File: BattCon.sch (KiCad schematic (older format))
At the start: 31 parts

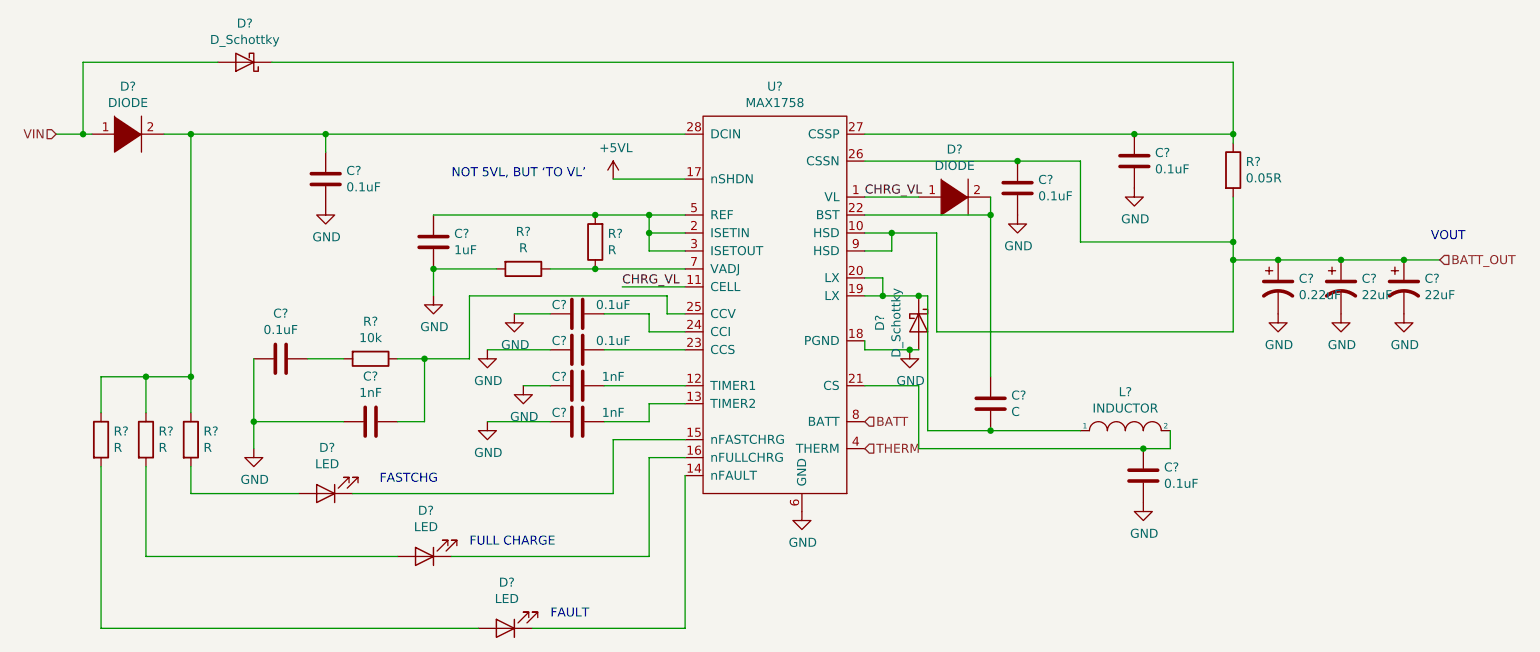
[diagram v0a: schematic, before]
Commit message: Schematics Done. Now need to do footprints
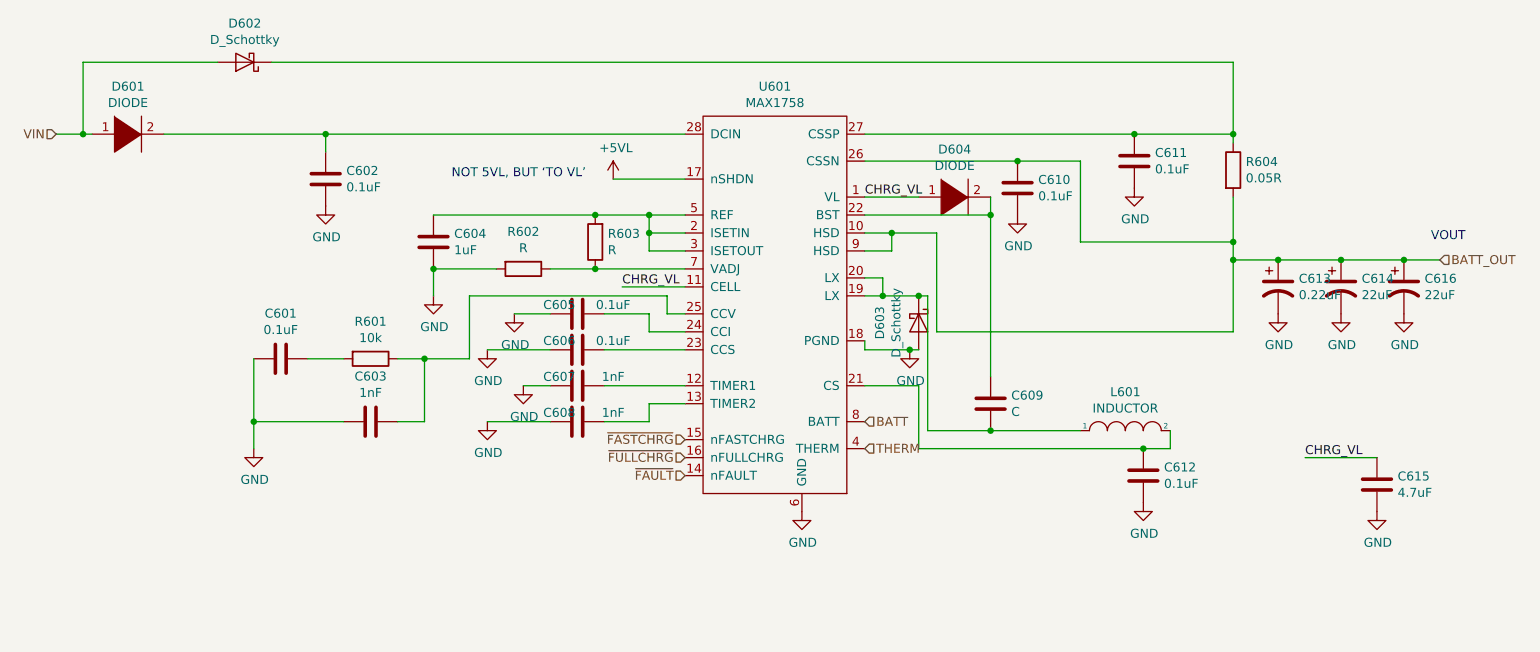
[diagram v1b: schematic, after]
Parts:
- removed D? (x3): LED, symbol Device:LED
- removed R? (x3): R, symbol Device:R
- added C615: 4.7uF, symbol Device:C
- R601, R602, R603, R604: renamed from R?; footprint (none) -> Resistor_SMD:R_0805_2012Metric
- gave numbers to parts that had none: 21
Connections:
- net CHRG_VL: now also C615.1
- net GND: now also C615.2
- net ~FASTCHRG: now reaches U601.15 (nFASTCHRG)
- net ~FULLCHRG: now reaches U601.16 (nFULLCHRG)
- net ~FAULT: now reaches U601.14 (nFAULT)
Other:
- note removed: "FASTCHG\n"
- note removed: "FAULT\n"
- note removed: "FULL CHARGE\n"

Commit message: Schematics done, now assigning footprints to do PCB Next
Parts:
- C601, C602, C603, C604, C605, C606, C607, C608, C609, C610, C611, C612, C613, C614, C615, C616: footprint (none) -> Capacitor_SMD:C_0805_2012Metric
- D601, D602, D603, D604: footprint (none) -> Diode_SMD:D_0805_2012Metric
- L601: footprint (none) -> Inductor_SMD:L_0805_2012Metric
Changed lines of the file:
@@
 F 0 "C605" V 5150 3650 50  0000 C CNN
 F 1 "0.1uF" V 5150 3950 50  0000 C CNN
-F 2 "" H 5238 3600 50  0001 C CNN
+F 2 "Capacitor_SMD:C_0805_2012Metric" H 5238 3600 50  0001 C CNN
 F 3 "~" H 5200 3750 50  0001 C CNN
 	1    5200 3750
@@
 F 0 "C606" V 5150 3850 50  0000 C CNN
 F 1 "0.1uF" V 5150 4150 50  0000 C CNN
-F 2 "" H 5238 3800 50  0001 C CNN
+F 2 "Capacitor_SMD:C_0805_2012Metric" H 5238 3800 50  0001 C CNN
 F 3 "~" H 5200 3950 50  0001 C CNN
 	1    5200 3950
@@
 F 0 "C607" V 5150 4050 50  0000 C CNN
 F 1 "1nF" V 5150 4350 50  0000 C CNN
-F 2 "" H 5238 4000 50  0001 C CNN
+F 2 "Capacitor_SMD:C_0805_2012Metric" H 5238 4000 50  0001 C CNN
 F 3 "~" H 5200 4150 50  0001 C CNN
 	1    5200 4150
@@
 F 0 "C603" V 3798 4350 50  0000 C CNN
 F 1 "1nF" V 3889 4350 50  0000 C CNN
-F 2 "" H 4088 4200 50  0001 C CNN
+F 2 "Capacitor_SMD:C_0805_2012Metric" H 4088 4200 50  0001 C CNN
 F 3 "~" H 4050 4350 50  0001 C CNN
 	1    4050 4350
@@
 F 0 "C601" V 3298 4000 50  0000 C CNN
 F 1 "0.1uF" V 3389 4000 50  0000 C CNN
-F 2 "" H 3588 3850 50  0001 C CNN
+F 2 "Capacitor_SMD:C_0805_2012Metric" H 3588 3850 50  0001 C CNN
 F 3 "~" H 3550 4000 50  0001 C CNN
 	1    3550 4000
@@
 F 0 "C604" H 4285 3304 50  0000 R CNN
 F 1 "1uF" H 4285 3395 50  0000 R CNN
-F 2 "" H 4438 3200 50  0001 C CNN
+F 2 "Capacitor_SMD:C_0805_2012Metric" H 4438 3200 50  0001 C CNN
 F 3 "~" H 4400 3350 50  0001 C CNN
 	1    4400 3350
@@
 F 0 "C602" H 3685 2954 50  0000 R CNN
 F 1 "0.1uF" H 3685 3045 50  0000 R CNN
-F 2 "" H 3838 2850 50  0001 C CNN
+F 2 "Capacitor_SMD:C_0805_2012Metric" H 3838 2850 50  0001 C CNN
 F 3 "~" H 3800 3000 50  0001 C CNN
 	1    3800 3000
@@
 F 0 "D601" H 2700 3015 50  0000 C CNN
 F 1 "DIODE" H 2700 2924 50  0000 C CNN
-F 2 "" H 2700 2750 50  0001 C CNN
+F 2 "Diode_SMD:D_0805_2012Metric" H 2700 2750 50  0001 C CNN
 F 3 "~" H 2700 2750 50  0001 C CNN
 	1    2700 2750
@@
 F 0 "D602" H 3350 2134 50  0000 C CNN
 F 1 "D_Schottky" H 3350 2225 50  0000 C CNN
-F 2 "" H 3350 2350 50  0001 C CNN
+F 2 "Diode_SMD:D_0805_2012Metric" H 3350 2350 50  0001 C CNN
 F 3 "~" H 3350 2350 50  0001 C CNN
 	1    3350 2350
@@
 F 0 "C611" H 8185 2854 50  0000 R CNN
 F 1 "0.1uF" H 8185 2945 50  0000 R CNN
-F 2 "" H 8338 2750 50  0001 C CNN
+F 2 "Capacitor_SMD:C_0805_2012Metric" H 8338 2750 50  0001 C CNN
 F 3 "~" H 8300 2900 50  0001 C CNN
 	1    8300 2900
@@
 F 0 "C610" H 7535 3004 50  0000 R CNN
 F 1 "0.1uF" H 7535 3095 50  0000 R CNN
-F 2 "" H 7688 2900 50  0001 C CNN
+F 2 "Capacitor_SMD:C_0805_2012Metric" H 7688 2900 50  0001 C CNN
 F 3 "~" H 7650 3050 50  0001 C CNN
 	1    7650 3050
@@
 F 0 "C613" H 9215 3646 50  0000 L CNN
 F 1 "0.22uF" H 9215 3555 50  0000 L CNN
-F 2 "" H 9100 3600 50  0001 C CNN
+F 2 "Capacitor_SMD:C_0805_2012Metric" H 9100 3600 50  0001 C CNN
 F 3 "~" H 9100 3600 50  0001 C CNN
 	1    9100 3600
@@
 F 0 "C614" H 9565 3646 50  0000 L CNN
 F 1 "22uF" H 9565 3555 50  0000 L CNN
-F 2 "" H 9450 3600 50  0001 C CNN
+F 2 "Capacitor_SMD:C_0805_2012Metric" H 9450 3600 50  0001 C CNN
 F 3 "~" H 9450 3600 50  0001 C CNN
 	1    9450 3600
@@
 F 0 "C616" H 9915 3646 50  0000 L CNN
 F 1 "22uF" H 9915 3555 50  0000 L CNN
-F 2 "" H 9800 3600 50  0001 C CNN
+F 2 "Capacitor_SMD:C_0805_2012Metric" H 9800 3600 50  0001 C CNN
 F 3 "~" H 9800 3600 50  0001 C CNN
 	1    9800 3600
@@
 F 0 "D604" H 7300 3365 50  0000 C CNN
 F 1 "DIODE" H 7300 3274 50  0000 C CNN
-F 2 "" H 7300 3100 50  0001 C CNN
+F 2 "Diode_SMD:D_0805_2012Metric" H 7300 3100 50  0001 C CNN
 F 3 "~" H 7300 3100 50  0001 C CNN
 	1    7300 3100
@@
 F 0 "C609" H 7385 4204 50  0000 R CNN
 F 1 "C" H 7385 4295 50  0000 R CNN
-F 2 "" H 7538 4100 50  0001 C CNN
+F 2 "Capacitor_SMD:C_0805_2012Metric" H 7538 4100 50  0001 C CNN
 F 3 "~" H 7500 4250 50  0001 C CNN
 	1    7500 4250
@@
 F 0 "L601" H 8250 4615 50  0000 C CNN
 F 1 "INDUCTOR" H 8250 4524 50  0000 C CNN
-F 2 "" H 8250 4400 50  0001 C CNN
+F 2 "Inductor_SMD:L_0805_2012Metric" H 8250 4400 50  0001 C CNN
 F 3 "~" H 8250 4400 50  0001 C CNN
 	1    8250 4400
@@
 F 0 "D603" H 7100 3584 50  0000 C CNN
 F 1 "D_Schottky" H 7100 3675 50  0000 C CNN
-F 2 "" H 7100 3800 50  0001 C CNN
+F 2 "Diode_SMD:D_0805_2012Metric" H 7100 3800 50  0001 C CNN
 F 3 "~" H 7100 3800 50  0001 C CNN
 	1    7100 3800
@@
 F 0 "C612" H 8465 4696 50  0000 L CNN
 F 1 "0.1uF" H 8465 4605 50  0000 L CNN
-F 2 "" H 8388 4500 50  0001 C CNN
+F 2 "Capacitor_SMD:C_0805_2012Metric" H 8388 4500 50  0001 C CNN
 F 3 "~" H 8350 4650 50  0001 C CNN
 	1    8350 4650
@@
 F 0 "C608" V 5150 4250 50  0000 C CNN
 F 1 "1nF" V 5150 4550 50  0000 C CNN
-F 2 "" H 5238 4200 50  0001 C CNN
+F 2 "Capacitor_SMD:C_0805_2012Metric" H 5238 4200 50  0001 C CNN
 F 3 "~" H 5200 4350 50  0001 C CNN
 	1    5200 4350
@@
 F 0 "C615" H 9765 4746 50  0000 L CNN
 F 1 "4.7uF" H 9765 4655 50  0000 L CNN
-F 2 "" H 9688 4550 50  0001 C CNN
+F 2 "Capacitor_SMD:C_0805_2012Metric" H 9688 4550 50  0001 C CNN
 F 3 "~" H 9650 4700 50  0001 C CNN
 	1    9650 4700

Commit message: Assigning footprints
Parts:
- U601: footprint (none) -> Package_SO:SSOP-28_5.3x10.2mm_P0.65mm
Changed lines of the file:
@@
 F 0 "U601" H 6300 4715 50  0000 C CNN
 F 1 "MAX1758" H 6300 4624 50  0000 C CNN
-F 2 "" H 6650 3600 50  0001 C CNN
+F 2 "Package_SO:SSOP-28_5.3x10.2mm_P0.65mm" H 6650 3600 50  0001 C CNN
 F 3 "" H 6650 3600 50  0001 C CNN
 	1    6500 3600

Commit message: updated layout
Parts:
- U601: symbol Roverschemlib:MAX1758 -> Mars-Rover-rescue:MAX1758-Roverschemlib
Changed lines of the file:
@@
 $EndComp
 $Comp
-L Roverschemlib:MAX1758 U601
+L Mars-Rover-rescue:MAX1758-Roverschemlib U601
 U 1 1 5C44D2A5
 P 6500 3600
